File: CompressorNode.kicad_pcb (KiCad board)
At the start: 2 copper layers, 129.5 x 85.1 mm, 34 parts, among them J1 EXT1, J10 Screw_Terminal_01x03, J11 Screw_Terminal_01x02, J12 Screw_Terminal_01x03, J13 Screw_Terminal_01x04, J2 Screw_Terminal_01x04, J3 Screw_Terminal_01x03, J4 EXT2, J5 Screw_Terminal_01x02, J6 Screw_Terminal_01x02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

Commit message: Labels on PCB corrected V0.13
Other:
- board text added: "Compressor/Laser cutter Node V0.13 Concept 2020 Makerspace Leiden"
- board text added: "White or Black"
- board text removed: "Compressor/Laser cutter Node V0.12 Concept 2020 Makerspace Leiden"
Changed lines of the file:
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@@
   (general
     (thickness 1.6)
-    (drawings 59)
+    (drawings 62)
     (tracks 174)
     (zones 0)
@@
   (title_block
     (title CompressorNode)
-    (date 2020-04-02)
-    (rev "V0.12 Concept")
+    (date 2020-04-04)
+    (rev "V0.13 Concept")
     (company "MakerSpace Leiden")
     (comment 1 "Getekend door Hans Beerman")
@@
     )
   )
+  (gr_text Red (at 104.14 79.375 90) (layer F.SilkS)
+    (effects (font (size 1.2 1.2) (thickness 0.3)))
+  )
+  (gr_text Yellow (at 99.06 80.645 90) (layer F.SilkS)
+    (effects (font (size 1.2 1.2) (thickness 0.3)))
+  )
+  (gr_text "White or Black" (at 94.615 84.455 90) (layer F.SilkS)
+    (effects (font (size 1.2 1.2) (thickness 0.3)))
+  )
   (gr_text 1 (at 144.145 80.645) (layer F.SilkS)
     (effects (font (size 1.2 1.2) (thickness 0.3)))
@@
     (effects (font (size 1.2 1.2) (thickness 0.3)))
   )
-  (gr_text "Compressor/Laser cutter Node\nV0.12 Concept 2020\nMakerspace Leiden" (at 190.5 124.46) (layer F.SilkS)
+  (gr_text "Compressor/Laser cutter Node\nV0.13 Concept 2020\nMakerspace Leiden" (at 190.5 124.46) (layer F.SilkS)
     (effects (font (size 1.7 1.7) (thickness 0.4)))
   )
@@
   )
   (gr_line (start 121.92 73.66) (end 119.38 68.58) (layer F.SilkS) (width 0.22))
-  (gr_text GND (at 123.825 71.12) (layer F.SilkS)
+  (gr_text GND (at 113.665 71.12) (layer F.SilkS)
     (effects (font (size 1.2 1.2) (thickness 0.3)))
   )
@@
     (effects (font (size 1.2 1.2) (thickness 0.3)))
   )
-  (gr_text +5V (at 113.03 71.12) (layer F.SilkS)
-    (effects (font (size 1.2 1.2) (thickness 0.3)))
-  )
-  (gr_text GND (at 104.775 71.12) (layer F.SilkS)
+  (gr_text +5V (at 123.825 71.12) (layer F.SilkS)
+    (effects (font (size 1.2 1.2) (thickness 0.3)))
+  )
+  (gr_text GND (at 94.615 71.12) (layer F.SilkS)
     (effects (font (size 1.2 1.2) (thickness 0.3)))
   )
@@
     (effects (font (size 1.2 1.2) (thickness 0.3)))
   )
-  (gr_text +3.3V (at 93.98 71.12) (layer F.SilkS)
-    (effects (font (size 1.2 1.2) (thickness 0.3)))
-  )
+  (gr_text +3.3V (at 104.775 71.12) (layer F.SilkS)
+    (effects (font (size 1.2 1.2) (thickness 0.3)))
+  )

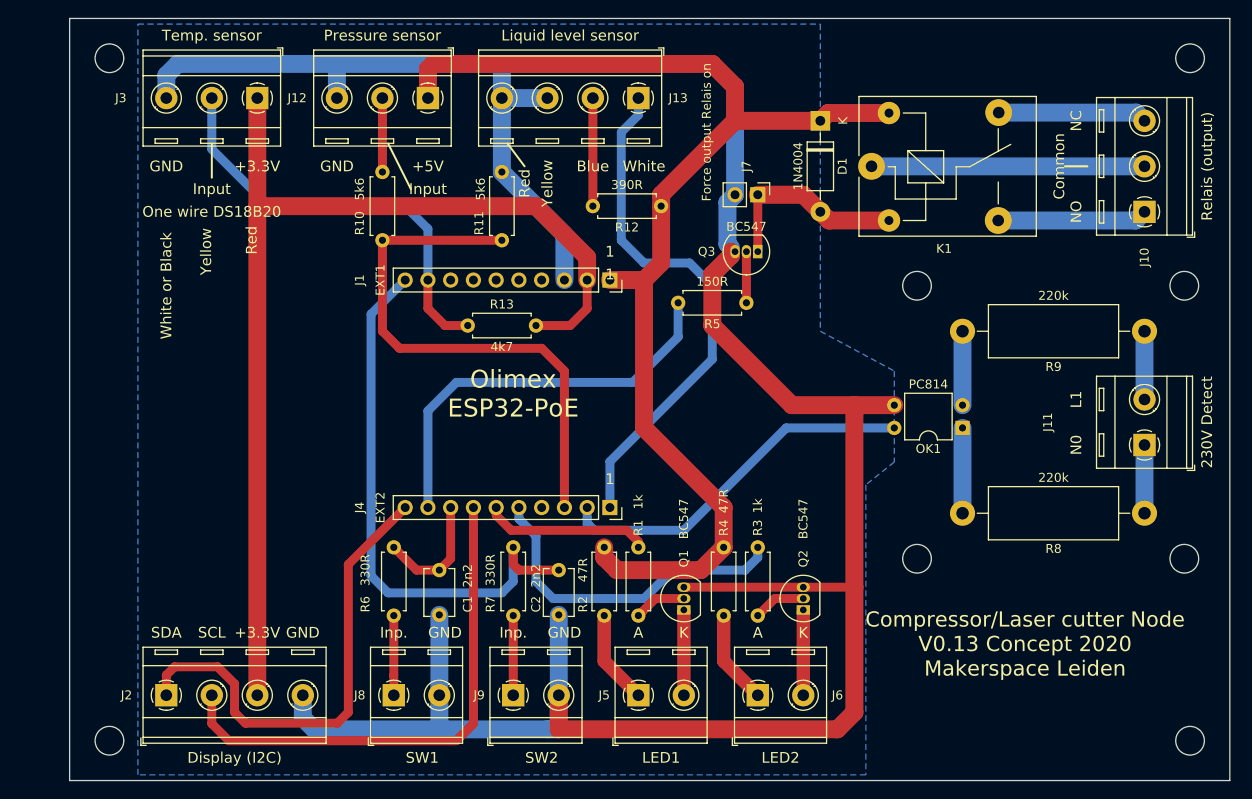
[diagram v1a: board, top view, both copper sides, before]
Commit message: Moved some screw terminals to make room for USB cable. Also added screw terminal for power (out) V0.14 Concept
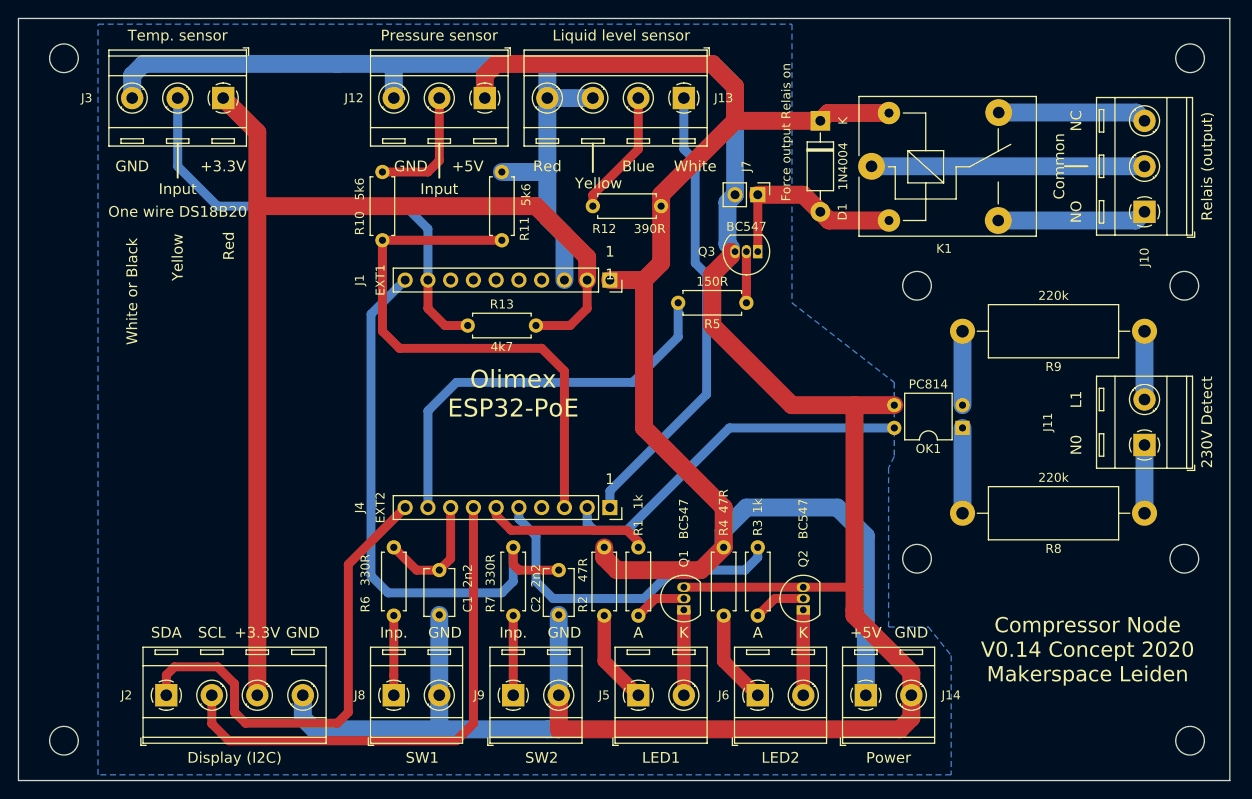
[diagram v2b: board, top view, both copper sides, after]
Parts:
- added J14: Screw_Terminal_01x02, TerminalBlock_RND:TerminalBlock_RND_205-00287_1x02_P5.08mm_Horizontal, F.Cu at (172.7, 130.2)
- moved J12 6.35 mm to (130.2, 63.5)
- moved J13 5.08 mm to (152.4, 63.5)
- moved J3 3.81 mm to (101.0, 63.5)
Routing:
- net +5V: track 135.6 -> 166.8 mm
- net GND: track 303.3 -> 319.7 mm
- net GPI39: track 58.4 -> 51.2 mm
- net Net-(J12-Pad2): track 8.25 -> 13.9 mm
- net GPIO4_U1TXD: track 47.7 -> 52.6 mm
- net Net-(J13-Pad2): track 12.1 -> 14.2 mm
- net +3V3: track 118.1 -> 119.7 mm
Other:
- board size 129.5 x 85.1 mm -> 135.3 x 85.1 mm
- board text added: "Compressor Node V0.14 Concept 2020 Makerspace Leiden"
- board text added: "Power"
- board text removed: "Compressor/Laser cutter Node V0.13 Concept 2020 Makerspace Leiden"

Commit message: Removed Power connector, added +5V output to the connectors for the switches V0.15 concept
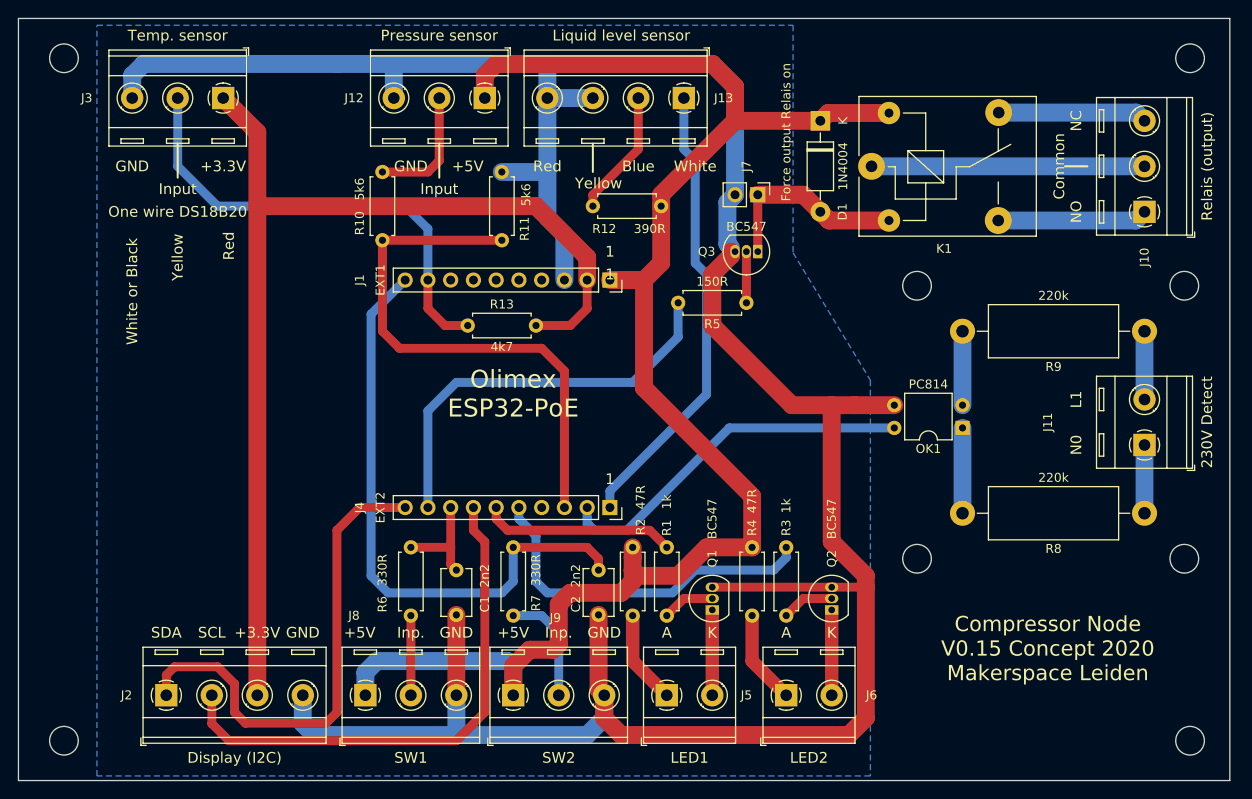
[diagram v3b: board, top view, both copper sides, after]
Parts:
- removed J14: Screw_Terminal_01x02, TerminalBlock_RND:TerminalBlock_RND_205-00287_1x02_P5.08mm_Horizontal
- J8, J9: value Screw_Terminal_01x02 -> Screw_Terminal_01x03; footprint TerminalBlock_RND:TerminalBlock_RND_205-00287_1x02_P5.08mm_Horizontal -> TerminalBlock_RND:TerminalBlock_RND_205-00288_1x03_P5.08mm_Horizontal
- moved C2 4.44 mm to (142.9, 116.2)
- moved J5 3.18 mm to (150.5, 130.2)
- moved J6 3.18 mm to (163.8, 130.2)
- moved R1 3.18 mm to (150.5, 121.3)
- moved R2 3.18 mm to (146.7, 113.7)
- moved R3 3.18 mm to (163.8, 121.3)
- moved R4 3.18 mm to (160.0, 113.7)
- moved J8 3.17 mm to (116.8, 130.2)
- moved Q1 3.17 mm to (155.6, 120.7)
- moved Q2 3.17 mm to (168.9, 120.7)
- moved C1 1.91 mm to (127.0, 116.2)
- moved R6 1.91 mm to (121.9, 121.3)
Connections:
- J8 pad 1: Net-(J8-Pad1) -> +5V
- J8 pad 2: GND -> Net-(J8-Pad2)
- J9 pad 1: Net-(J9-Pad1) -> +5V
- J9 pad 2: GND -> Net-(J9-Pad2)
- R6 pad 1: Net-(J8-Pad1) -> Net-(J8-Pad2)
- R7 pad 1: Net-(J9-Pad1) -> Net-(J9-Pad2)
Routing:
- net Net-(J9-Pad2): track 0.00 -> 12.9 mm
- net +5V: track 166.8 -> 178.9 mm
- net Net-(J9-Pad1): track 8.89 -> 0.00 mm
- net Net-(J8-Pad2): track 0.00 -> 8.89 mm
- net Net-(J8-Pad1): track 8.89 -> 0.00 mm
- net GND: track 319.7 -> 312.5 mm
- net GPIO5_SPI_C5: track 62.8 -> 66.9 mm
- net GPIO32: track 18.6 -> 21.6 mm
- net GPIO33: track 37.6 -> 40.3 mm
- net GPIO13_I2C-SDA: track 53.4 -> 55.6 mm
- net GPIO15_HS2_CMD: track 13.6 -> 11.7 mm
- net GPIO16_I2C-SCL: track 58.1 -> 59.1 mm
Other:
- board text added: "Compressor Node V0.15 Concept 2020 Makerspace Leiden"
- board text removed: "Compressor Node V0.14 Concept 2020 Makerspace Leiden"
- board text removed: "Power"

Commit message: V0.16 concept: LED in switches are switched on or off to show which one can be pressed
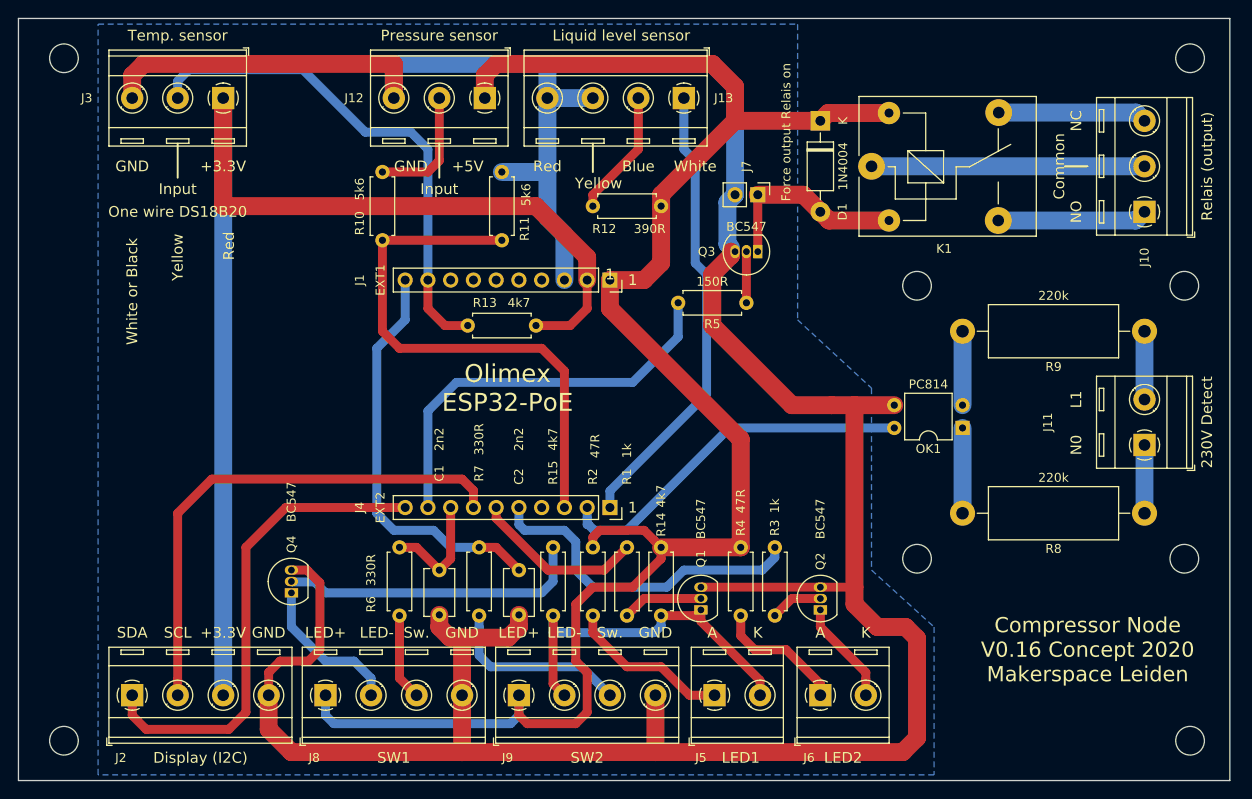
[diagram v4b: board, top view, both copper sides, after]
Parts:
- added Q4: BC547, Package_TO_SOT_THT:TO-92_Inline, F.Cu at (108.6, 118.7)
- added R14: 4k7, Resistor_THT:R_Axial_DIN0207_L6.3mm_D2.5mm_P7.62mm_Horizontal, F.Cu at (149.9, 113.7)
- added R15: 4k7, Resistor_THT:R_Axial_DIN0207_L6.3mm_D2.5mm_P7.62mm_Horizontal, F.Cu at (137.8, 113.7)
- J8, J9: value Screw_Terminal_01x03 -> Screw_Terminal_01x04; footprint TerminalBlock_RND:TerminalBlock_RND_205-00288_1x03_P5.08mm_Horizontal -> TerminalBlock_RND:TerminalBlock_RND_205-00289_1x04_P5.08mm_Horizontal
- moved C2 8.89 mm to (134.0, 116.2)
- moved J5 5.33 mm to (155.8, 130.2)
- moved J8 4.45 mm to (112.4, 130.2)
- moved R1 4.44 mm to (146.1, 121.3)
- moved R2 4.44 mm to (142.2, 113.7)
- moved R7 3.81 mm to (129.5, 121.3)
- moved J2 3.81 mm to (90.8, 130.2)
- moved J6 3.81 mm to (167.6, 130.2)
- moved C1 1.91 mm to (125.1, 116.2)
- moved Q2 1.27 mm to (167.6, 120.7)
- moved R3 1.27 mm to (162.6, 121.3)
- moved R4 1.27 mm to (158.8, 113.7)
- moved R6 1.27 mm to (120.7, 121.3)
- moved Q1 1.27 mm to (154.3, 120.7)
- moved J9 0.64 mm to (134.0, 130.2)
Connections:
- J5 pad 2: Net-(J5-Pad2) -> SWITCH-LED1-
- J8 pad 3: GND -> Net-(J8-Pad3)
- J9 pad 2: Net-(J9-Pad2) -> SWITCH-LED1-
- J9 pad 3: GND -> Net-(J9-Pad3)
- Q1 pad 1: Net-(J5-Pad2) -> SWITCH-LED1-
- R6 pad 1: Net-(J8-Pad2) -> Net-(J8-Pad3)
- R7 pad 1: Net-(J9-Pad2) -> Net-(J9-Pad3)
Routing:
- net GND: track 312.5 -> 355.2 mm
- net SWITCH-LED1-: track 0.00 -> 41.8 mm
- net Net-(Q4-Pad2): track 0.00 -> 34.1 mm
- net GPIO5_SPI_C5: track 66.9 -> 45.9 mm
- net Net-(J9-Pad3): track 0.00 -> 20.9 mm
- net +5V: track 178.9 -> 197.0 mm
- net +3V3: track 119.7 -> 134.0 mm
- net Net-(J9-Pad2): track 12.9 -> 0.00 mm
- net Net-(J8-Pad3): track 0.00 -> 9.68 mm
- net Net-(J5-Pad2): track 9.32 -> 0.00 mm
- net Net-(J8-Pad2): track 8.89 -> 17.0 mm
- net Net-(J5-Pad1): track 10.5 -> 18.4 mm
- net GPIO4_U1TXD: track 52.6 -> 57.1 mm
- net Net-(J6-Pad1): track 10.5 -> 14.6 mm
- net Net-(Q1-Pad2): track 5.87 -> 9.04 mm
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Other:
- board text added: "Compressor Node V0.16 Concept 2020 Makerspace Leiden"
- board text added: "LED+"
- board text added: "LED-"
- board text added: "Sw."
- board text removed: "Compressor Node V0.15 Concept 2020 Makerspace Leiden"
- board text removed: "Inp."

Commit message: Changed some labels and R15 chanched to 47k V0.18
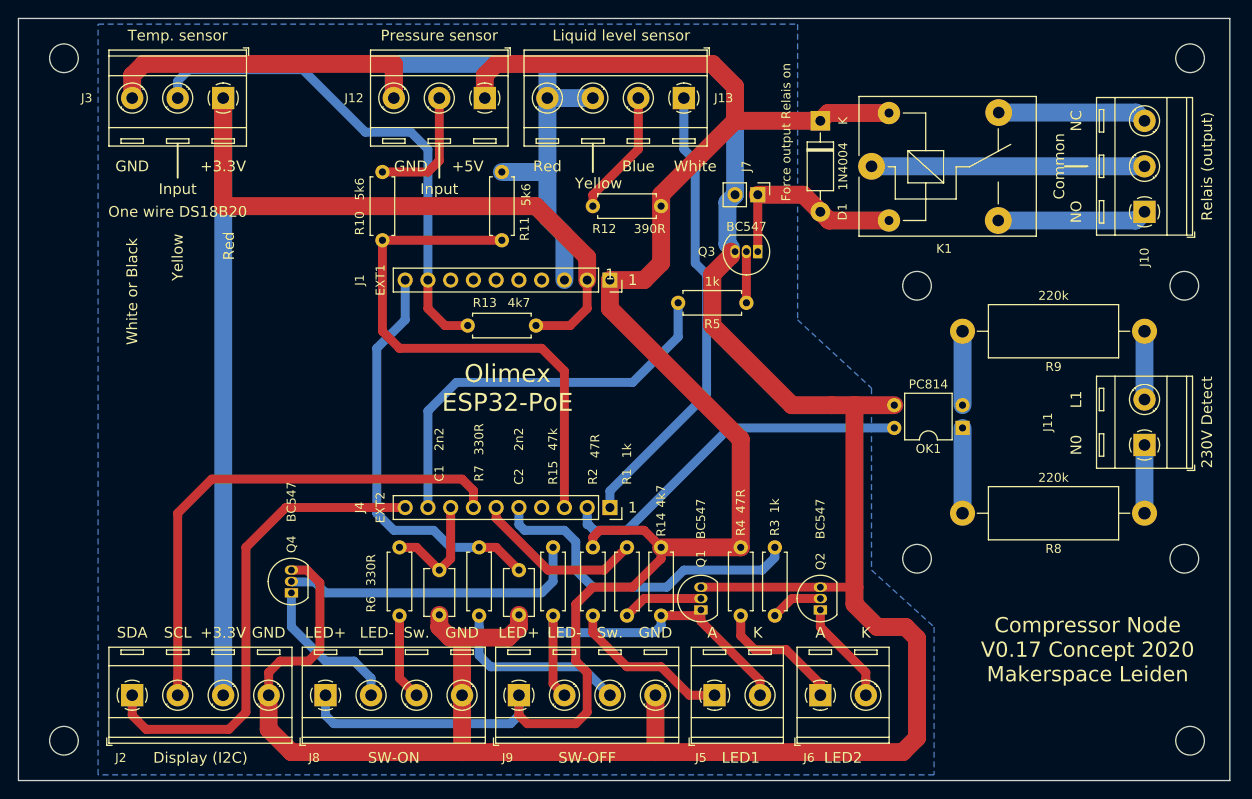
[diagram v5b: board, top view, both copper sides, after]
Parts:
- R15: value 4k7 -> 47k
- R5: value 150R -> 1k
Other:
- board text added: "Compressor Node V0.17 Concept 2020 Makerspace Leiden"
- board text added: "SW-OFF"
- board text added: "SW-ON"
- board text removed: "Compressor Node V0.16 Concept 2020 Makerspace Leiden"
- board text removed: "SW1"
- board text removed: "SW2"
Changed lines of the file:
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@@
   (title_block
     (title CompressorNode)
-    (date 2020-04-20)
-    (rev "V0.16 Concept")
+    (date 2020-04-27)
+    (rev "V0.17 Concept")
     (company "MakerSpace Leiden")
     (comment 1 "Getekend door Hans Beerman")
@@
       (effects (font (size 1 1) (thickness 0.15)) (justify left))
     )
-    (fp_text value 4k7 (at -12.065 0 90) (layer F.SilkS)
+    (fp_text value 47k (at -12.065 0 90) (layer F.SilkS)
       (effects (font (size 1 1) (thickness 0.15)))
     )
@@
       (effects (font (size 1 1) (thickness 0.15)))
     )
-    (fp_text value 150R (at 3.81 2.37) (layer F.SilkS)
+    (fp_text value 1k (at 3.81 2.37) (layer F.SilkS)
       (effects (font (size 1 1) (thickness 0.15)))
     )
@@
     (effects (font (size 1.2 1.2) (thickness 0.3)))
   )
-  (gr_text "Compressor Node\nV0.16 Concept 2020\nMakerspace Leiden" (at 197.485 125.095) (layer F.SilkS)
+  (gr_text "Compressor Node\nV0.17 Concept 2020\nMakerspace Leiden" (at 197.485 125.095) (layer F.SilkS)
     (effects (font (size 1.7 1.7) (thickness 0.4)))
   )
@@
     (effects (font (size 1.2 1.2) (thickness 0.3)))
   )
-  (gr_text SW2 (at 141.605 137.16) (layer F.SilkS)
-    (effects (font (size 1.2 1.2) (thickness 0.3)))
-  )
-  (gr_text SW1 (at 120.015 137.16) (layer F.SilkS)
-    (effects (font (size 1.2 1.2) (thickness 0.3)))
-  )
+  (gr_text SW-OFF (at 141.605 137.16) (layer F.SilkS)
+    (effects (font (size 1.2 1.2) (thickness 0.3)))
+  )
+  (gr_text SW-ON (at 120.015 137.16) (layer F.SilkS)
+    (effects (font (size 1.2 1.2) (thickness 0.3)))
+  )

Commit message: V0.18: added a screw connector for safety, to switch of compressor in case a cable is disconnected
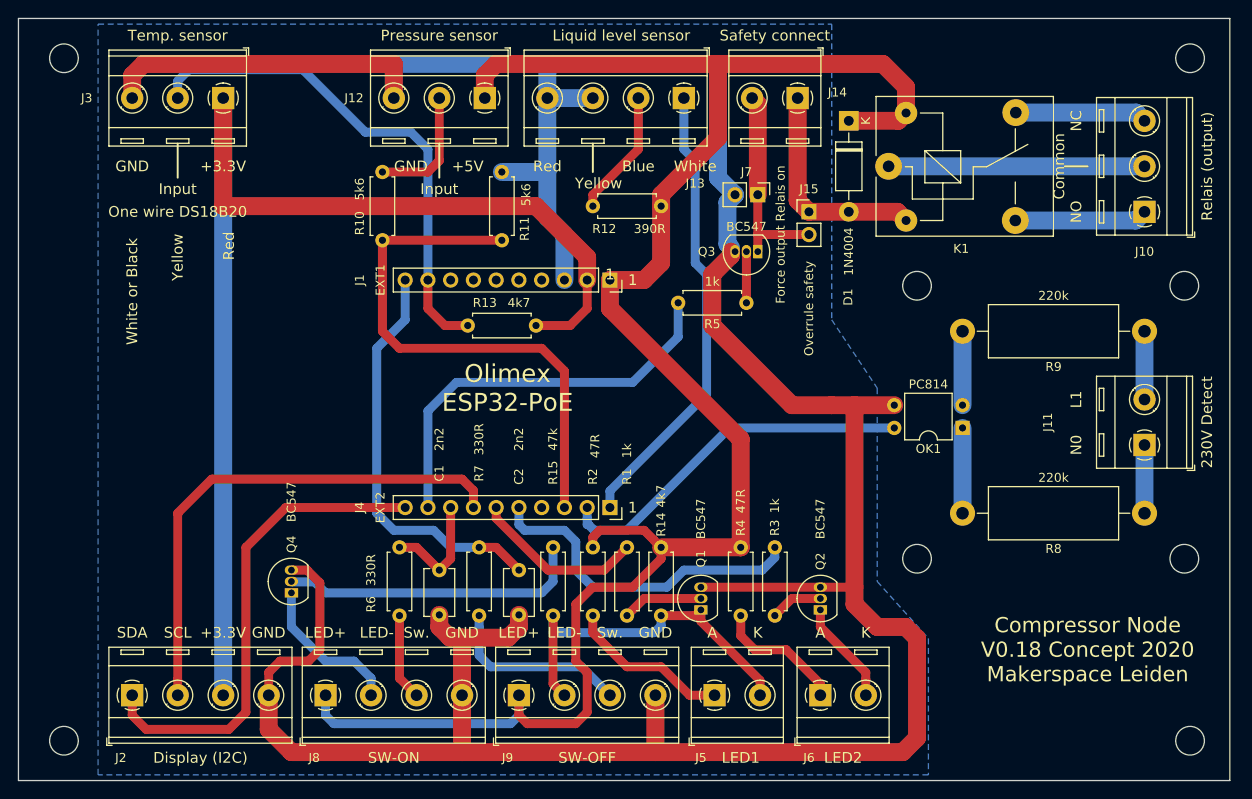
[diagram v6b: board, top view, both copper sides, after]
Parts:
- added J14: Screw_Terminal_01x02, TerminalBlock_RND:TerminalBlock_RND_205-00287_1x02_P5.08mm_Horizontal, F.Cu at (165.1, 63.5)
- added J15: Overrule safety, Connector_PinHeader_2.54mm:PinHeader_1x02_P2.54mm_Vertical, F.Cu at (166.4, 76.2)
- moved D1 3.18 mm to (170.8, 66.0)
- moved K1 1.91 mm to (175.3, 71.1)
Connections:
- J7 pad 1: Net-(D1-Pad2) -> Net-(J14-Pad2)
- Q3 pad 1: Net-(D1-Pad2) -> Net-(J14-Pad2)
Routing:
- net Net-(J14-Pad2): track 0.00 -> 23.1 mm
- net +5V: track 197.0 -> 210.0 mm
- net Net-(D1-Pad2): track 22.2 -> 24.5 mm
- net Net-(J10-Pad1): track 16.7 -> 14.8 mm
- net Net-(J10-Pad2): track 30.5 -> 28.6 mm
- net Net-(J10-Pad3): track 16.7 -> 14.8 mm
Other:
- board text added: "Compressor Node V0.18 Concept 2020 Makerspace Leiden"
- board text added: "Safety connect"
- board text removed: "Compressor Node V0.17 Concept 2020 Makerspace Leiden"
